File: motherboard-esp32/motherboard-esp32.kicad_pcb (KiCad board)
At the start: 4 copper layers, 300 x 70 mm, 42 parts, among them J3 JST_2P_XH, Q1 DOD4185, Q2 DOD4185, Q3 DOD4185, U1 LMR23630AFDDAR, U2 LM25085MY/NOPB

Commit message: split into two boards for dc/dc converter
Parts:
- removed C10: 1nF, bio-robot:C_0603_1608Metric
- removed C11: 3.3nF, bio-robot:C_0603_1608Metric
- removed C12: 47uF, bio-robot:CAP_EEEFT1H470AP
- removed C7, C8: 22u_1206, bots:C_1206_3216Metric
- removed C9: 0.47u, bio-robot:C_0603_1608Metric
- removed D2: STPS20M100SG-TR, bio-robot:TO-263-2
- removed L2: 3.3uH, bio-robot:IND_MDA1050-3R3M
- removed Q3: DOD4185, bio-robot:DPAK-3_ONS
- removed R3: 113k, bio-robot:R_0603_1608Metric
- removed R4: 4.12k, bio-robot:R_0603_1608Metric
- removed R5: 10m, bio-robot:R_0805_2012Metric
- removed R8: 10k, bio-robot:R_0603_1608Metric
- removed R9: 2.26k, bio-robot:R_0603_1608Metric
- removed U2: LM25085MY/NOPB, bio-robot:MSOP8_PowerPad
- added H5: MountingHoleM3, MountingHole:MountingHole_3.2mm_M3_DIN965_Pad, F.Cu at (169.5, 29.0)
- added H6: MountingHoleM3, MountingHole:MountingHole_3.2mm_M3_DIN965_Pad, F.Cu at (169.5, 59.0)
- added H7: MountingHoleM3, MountingHole:MountingHole_3.2mm_M3_DIN965_Pad, F.Cu at (144.5, 29.0)
- added H8: MountingHoleM3, MountingHole:MountingHole_3.2mm_M3_DIN965_Pad, F.Cu at (144.5, 59.0)
- added P1: 1.8mm_16AWG, bio-robot:SolderPad_TH_16AWG_1.8mm, F.Cu at (143.5, 39.0)
- added P2: 1.8mm_16AWG, bio-robot:SolderPad_TH_16AWG_1.8mm, F.Cu at (143.5, 49.5)
- added P3: 1.8mm_16AWG, bio-robot:SolderPad_TH_16AWG_1.8mm, F.Cu at (162.5, 59.5)
- added P4: 1.8mm_16AWG, bio-robot:SolderPad_TH_16AWG_1.8mm, F.Cu at (152.0, 59.5)
- C5: moved to B.Cu
- moved C1 5.18 mm to (147.0, 78.5)
- moved C6 4.92 mm to (160.5, 68.5)
- moved R2 4.03 mm to (158.0, 85.0)
- moved L1 3.69 mm to (150.0, 70.0)
- moved C3 3.35 mm to (159.5, 78.0)
- moved C4 3.35 mm to (149.0, 82.5)
- moved R6 3.35 mm to (149.0, 84.0)
- moved R7 3.35 mm to (152.0, 84.0)
- moved U1 3.35 mm to (154.4, 79.6)
- moved C2 3.16 mm to (165.5, 78.5)
- moved C5 3.15 mm to (151.0, 80.4), turned to 0 degrees
- moved H2 2.50 mm to (54.5, 91.0)
- moved R1 2.24 mm to (158.0, 85.5)
- moved H1 2.00 mm to (54.5, 29.0)
- moved H4 1.58 mm to (343.0, 29.0)
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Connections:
- net Net-(BT1-PadP-) renamed /Power Input/P2+
- net Net-(BT2-PadP-) renamed /Power Input/P3+
- net Net-(BT4-PadP-) renamed /Power Input/P5+
- net Net-(BT5-PadP-) renamed /Power Input/P6+
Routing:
- net /dc-dc/U1_VCC: track 0.00 -> 4.91 mm, vias 0 -> 1
- net GND: vias 0 -> 45
- net /Power Input/VBAT: vias 0 -> 45
- added copper zone on F.Cu, net /Power Input/P2+
- added copper zone on F.Cu, net /Power Input/P3+
- added copper zone on B.Cu, net /Power Input/P5+
- added copper zone on B.Cu, net /Power Input/P6+
- added copper zone on B.Cu, net /Power Input/VBAT
- added copper zone on F.Cu, net /Power Input/VBAT
- added copper zone on B.Cu, net GND
- added copper zone on F.Cu, net GND
- added copper zone on In2.Cu, net GND
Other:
- board size 300 x 70 mm -> 296.5 x 70 mm
- board text added: "6.8V"
- board text added: "GND"
- board text added: "VCC"

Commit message: update
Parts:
- removed BT1, BT2, BT3, BT4, BT5, BT6: Keystone_254_BatteryClip_Holder, bio-robot:BAT_254_18650_Holder
- removed R7: 22.1k, bio-robot:R_0603_1608Metric
- added BT8: Keystone_1048P_DualBatteryHolder, bio-robot:BAT_1048P, F.Cu at (97.0, 39.5)
- added D2: SMAZ3V6, bots:D_SMA, F.Cu at (157.6, 52.5)
- added F1: 0437005.WR, bio-robot:Fuse_1206_3216Metric, F.Cu at (141.2, 54.3)
- added J2: Screw_Terminal_01x02, bio-robot:TerminalBlock_MaiXu_MX126-5.0-02P_1x02_P5.00mm, F.Cu at (167.2, 55.8)
- added J4: JST_2P_XH, bio-robot:JST_B2B-XH-A_LF__SN_, F.Cu at (71.5, 91.0)
- added J5: Screw_Terminal_01x02, bio-robot:TerminalBlock_MaiXu_MX126-5.0-02P_1x02_P5.00mm, F.Cu at (167.3, 67.2)
- added J6: Screw_Terminal_01x02, bio-robot:TerminalBlock_MaiXu_MX126-5.0-02P_1x02_P5.00mm, F.Cu at (167.3, 78.8)
- added J7: XT60, bio-robot:AMASS_XT60PW-M, F.Cu at (61.5, 77.8)
- added Q3: DOD4185, bio-robot:DPAK-3_ONS, F.Cu at (147.6, 51.7)
- added Q4: DOD4185, bio-robot:DPAK-3_ONS, F.Cu at (167.1, 48.5)
- added R3: 100k, bio-robot:R_0603_1608Metric, F.Cu at (154.4, 57.8)
- added R4: 100k, bio-robot:R_0603_1608Metric, F.Cu at (154.0, 46.8)
- added R5: 88.7k, bio-robot:R_0603_1608Metric, F.Cu at (153.1, 43.3)
- C1: value 0.1u -> 25SVPF100M; footprint bio-robot:C_0603_1608Metric -> bio-robot:CAP_25SVPF100M
- C2: value 25SVPF100M -> 10u; footprint bio-robot:CAP_25SVPF100M -> bio-robot:C_0805_2012Metric
- C3: value 10u -> 2.2u
- C4: value 30p -> 0.1u
- C5: value 2.2u -> 30p; footprint bio-robot:C_0805_2012Metric -> bio-robot:C_0603_1608Metric; moved to F.Cu
- H1, H2, H3, H4, H5, H6, H7, H8: footprint MountingHole:MountingHole_3.2mm_M3_DIN965_Pad -> bio-robot:MountingHole_3.2mm_M3_DIN965_Pad
- Q2, R1: moved to F.Cu
- R6: value 88.7k -> 22.1k
- moved J3 278.6 mm to (63.0, 90.7), turned to 0 degrees
- moved H4 172.9 mm to (170.2, 21.5)
- moved H3 172.8 mm to (170.2, 90.5)
- moved R2 71.8 mm to (88.3, 67.5)
- moved Q2 69.9 mm to (101.5, 69.2), turned to -90 degrees
- moved R1 69.6 mm to (88.8, 78.5), turned to 180 degrees
- moved D1 68.6 mm to (91.6, 72.7)
- moved F2 68.5 mm to (75.6, 75.2)
- moved Q1 68.2 mm to (81.8, 72.4)
- moved H7 66.9 mm to (117.2, 90.2), turned to 0 degrees
- moved H5 63.5 mm to (117.2, 65.2), turned to 0 degrees
- moved P1 54.6 mm to (127.2, 91.2), turned to 90 degrees
- moved C1 46.8 mm to (168.8, 37.1)
- moved C4 45.8 mm to (151.3, 36.8), turned to 90 degrees
- moved R6 42.9 mm to (156.2, 41.7)
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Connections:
- C1 pad 1: /dc-dc/BOOT -> +BATT
- C1 pad 2: /dc-dc/LM_OUT -> GND
- C2 pad 1: VCC -> +BATT
- C3 pad 1: VCC -> /dc-dc/U1_VCC
- C4 pad 1: +5V -> /dc-dc/BOOT
- C4 pad 2: /dc-dc/FB -> /dc-dc/LM_OUT
- C5 pad 1: /dc-dc/U1_VCC -> +5V
- C5 pad 2: GND -> /dc-dc/FB
- J3 pad 2: GND -> GNDPWR
- P2 pad 1: GND -> GNDPWR
- P4 pad 1: GND -> GNDPWR
- R6 pad 1: +5V -> /dc-dc/FB
- R6 pad 2: /dc-dc/FB -> GND
- U1 pad 5: VCC -> +BATT
- U1 pad 7: VCC -> +BATT
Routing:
- net +5V: track 0.00 -> 26.4 mm, vias 0 -> 46
- net /Power Input/VGATE_2: track 0.00 -> 24.3 mm, vias 0 -> 3
- net /Power Input/VGATE: track 0.00 -> 24.3 mm, vias 0 -> 3
- net /Power Input/SW2: track 0.00 -> 22.5 mm, vias 0 -> 2
- net /dc-dc/FB: track 0.00 -> 4.72 mm
- net /dc-dc/BOOT: track 0.00 -> 3.69 mm
- net GND: track 0.00 -> 1.30 mm, vias 45 -> 64
- net /dc-dc/U1_VCC: track 4.91 -> 5.57 mm, vias 1 -> 0
- net /Power Input/VBAT: vias 45 -> 0
- added copper zone on F.Cu, net +5V
- added copper zone on In2.Cu, net +5V
- added copper zone on F.Cu, net +BATT
- added copper zone on F.Cu, net /Power Input/BAT5V_MID
- added copper zone on F.Cu, net /Power Input/FUSE_BAT5V
- added copper zone on F.Cu, net /Power Input/FUSE_VCC
- added copper zone on F.Cu, net /Power Input/VBAT5V
- added copper zone on F.Cu, net /Power Input/VBAT5V_P2
- added copper zone on F.Cu, net /Power Input/VCC_MID
- added copper zone on F.Cu, net /dc-dc/LM_OUT
- added copper zone on In1.Cu, net GND
- removed copper zone on F.Cu, net /Power Input/P2+
- removed copper zone on F.Cu, net /Power Input/P3+
- removed copper zone on B.Cu, net /Power Input/P5+
- removed copper zone on B.Cu, net /Power Input/P6+
- removed copper zone on B.Cu, net /Power Input/VBAT
- removed copper zone on F.Cu, net /Power Input/VBAT
- removed copper zone on B.Cu, net GND
- removed copper zone on In2.Cu, net GND
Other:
- board size 296.5 x 70 mm -> 123.8 x 77 mm

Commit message: update
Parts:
- D1: footprint bio-robot:D_SMA -> bots:D_SMA
- J3, J4: footprint bio-robot:JST_B2B-XH-A_LF__SN_ -> bots:JST_B2B-XH-A_LF__SN_
- Q1, Q2, Q3, Q4: footprint bio-robot:DPAK-3_ONS -> bots:DPAK-3_ONS
- R1, R2, R3, R4: footprint bio-robot:R_0603_1608Metric -> bots:R_0603_1608Metric
- moved J4 26.9 mm to (64.3, 65.1)
- moved J3 26.8 mm to (55.0, 65.2)
- moved P2 24.3 mm to (117.5, 77.7)
- moved P1 21.8 mm to (117.5, 71.7)
- moved P3 5.51 mm to (148.0, 77.7)
- moved P4 1.03 mm to (148.0, 83.7)
- moved Q4 0.25 mm to (167.3, 48.5)
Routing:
- net /Power Input/SW2: track 22.5 -> 108.4 mm, vias 2 -> 4
- net GND: track 1.30 -> 79.9 mm, vias 64 -> 66
- net /Power Input/SW: track 0.00 -> 52.8 mm, vias 0 -> 2
- net GNDPWR: track 0.00 -> 17.1 mm, vias 0 -> 1
- net /Power Input/VGATE: track 24.3 -> 22.0 mm, vias 3 -> 2
- net /Power Input/VGATE_2: track 24.3 -> 22.1 mm, vias 3 -> 2
- net +5V: track 26.4 -> 27.3 mm, vias 46 -> 45
- net VCC: vias 0 -> 45
- added copper zone on F.Cu, net +6.8V
- added copper zone on F.Cu, net /Power Input/VBAT
- added copper zone on In1.Cu, net GNDPWR
- added copper zone on F.Cu, net VCC
- added copper zone on In2.Cu, net VCC
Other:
- outline, holes or cut-outs redrawn
- board text added: "12V_SW"
- board text added: "5V_SW"

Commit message: board files
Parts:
- moved H1 0.71 mm to (54.0, 21.0)
- moved H2 0.71 mm to (54.0, 91.0)
- moved H3 0.71 mm to (170.8, 91.0)
- moved H4 0.71 mm to (170.8, 21.0)
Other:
- outline, holes or cut-outs redrawn
- board text added: "Battery Motherboard MECH 540 / EECE 571M Marine Robotics Group 3: Quiet Bio-inspired Propulsion System Designed By: Henry Bryant Printed on: March 24th, 2026"
- board text added: "This board has two battery inputs. - 5V Rail: 2-Cell 18650 Protected (Li-Ion). Buck to 5V 3A. - 12V Rail: 3-Cell Custom Battery Pack using XT60. Buck to 6.8V, 10A."
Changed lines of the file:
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@@
 	(footprint "bio-robot:MountingHole_3.2mm_M3_DIN965_Pad"
 		(layer "F.Cu")
-		(at 170.25 90.5 90)
+		(at 170.75 91 90)
 		(descr "Mounting Hole 3.2mm, M3, generated by kicad-footprint-generator mountinghole.py")
 		(tags "mountinghole M3 DIN965")
@@
 				(pts
 					(arc
-						(start 170.25 94.5)
-						(mid 170.25 86.5)
-						(end 170.25 94.5)
+						(start 170.75 95)
+						(mid 170.75 87)
+						(end 170.75 95)
 					)
 				)
@@
 	(footprint "bio-robot:MountingHole_3.2mm_M3_DIN965_Pad"
 		(layer "F.Cu")
-		(at 54.5 21.5)
+		(at 54 21)
 		(descr "Mounting Hole 3.2mm, M3, generated by kicad-footprint-generator mountinghole.py")
 		(tags "mountinghole M3 DIN965")
@@
 				(pts
 					(arc
-						(start 50.5 21.5)
-						(mid 58.5 21.5)
-						(end 50.5 21.5)
+						(start 50 21)
+						(mid 58 21)
+						(end 50 21)
 					)
 				)
@@
 	(footprint "bio-robot:MountingHole_3.2mm_M3_DIN965_Pad"
 		(layer "F.Cu")
-		(at 170.25 21.5)
+		(at 170.75 21)
 		(descr "Mounting Hole 3.2mm, M3, generated by kicad-footprint-generator mountinghole.py")
 		(tags "mountinghole M3 DIN965")
 		(property "Reference" "H4"
-			(at 2.699022 2.952848 0)
+			(at 2.25 3.5 0)
 			(layer "F.SilkS")
 			(effects
@@
 				(pts
 					(arc
-						(start 166.25 21.5)
-						(mid 174.25 21.5)
-						(end 166.25 21.5)
+						(start 166.75 21)
+						(mid 174.75 21)
+						(end 166.75 21)
 					)
 				)
@@
 	(footprint "bio-robot:MountingHole_3.2mm_M3_DIN965_Pad"
 		(layer "F.Cu")
-		(at 54.5 90.5)
+		(at 54 91)
 		(descr "Mounting Hole 3.2mm, M3, generated by kicad-footprint-generator mountinghole.py")
 		(tags "mountinghole M3 DIN965")
@@
 				(pts
 					(arc
-						(start 50.5 90.5)
-						(mid 58.5 90.5)
-						(end 50.5 90.5)
+						(start 50 91)
+						(mid 58 91)
+						(end 50 91)
 					)
 				)
@@
 	)
 	(gr_line
-		(start 50.5 21.5)
-		(end 50.5 90.5)
+		(start 50.5 21)
+		(end 50.5 91)
 		(stroke
 			(width 0.1)
@@
 	)
 	(gr_arc
-		(start 50.5 21.5)
-		(mid 51.671573 18.671573)
-		(end 54.5 17.5)
+		(start 50.5 21)
+		(mid 51.525126 18.525126)
+		(end 54 17.5)
 		(stroke
 			(width 0.1)
@@
 	)
 	(gr_arc
-		(start 54.5 94.5)
-		(mid 51.671573 93.328427)
-		(end 50.5 90.5)
+		(start 54 94.5)
+		(mid 51.525126 93.474874)
+		(end 50.5 91)
 		(stroke
-			(width 0.1)
-			(type default)
+			(width 0.15)
+			(type solid)
 		)
 		(layer "Edge.Cuts")
 	)
 	(gr_line
-		(start 54.5 94.5)
-		(end 170.25 94.5)
+		(start 54 94.5)
+		(end 170.75 94.5)
 		(stroke
 			(width 0.1)
@@
 	)
 	(gr_line
-		(start 170.25 17.5)
-		(end 54.5 17.5)
+		(start 170.75 17.5)
+		(end 54 17.5)
 		(stroke
 			(width 0.1)
@@
 	)
 	(gr_arc
-		(start 170.25 17.5)
-		(mid 173.078427 18.671573)
-		(end 174.25 21.5)
+		(start 170.75 17.5)
+		(mid 173.224874 18.525126)
+		(end 174.25 21)
 		(stroke
 			(width 0.1)
@@
 	)
 	(gr_arc
-		(start 174.25 90.5)
-		(mid 173.078427 93.328427)
-		(end 170.25 94.5)
+		(start 174.25 91)
+		(mid 173.224874 93.474874)
+		(end 170.75 94.5)
 		(stroke
 			(width 0.1)
@@
 	)
 	(gr_line
-		(start 174.25 90.5)
-		(end 174.25 21.5)
+		(start 174.25 91)
+		(end 174.25 21)
 		(stroke
 			(width 0.1)
@@
 		(layer "Edge.Cuts")
 	)
+	(gr_text "This board has two battery inputs.\n- 5V Rail: 2-Cell 18650 Protected (Li-Ion). \n	Buck to 5V 3A.\n- 12V Rail: 3-Cell Custom Battery Pack using XT60. \n	Buck to 6.8V, 10A."
+		(at 71.5 91.25 0)
+		(layer "F.SilkS")
+		(effects
+			(font
+				(size 1 1)
+				(thickness 0.15)
+			)
+			(justify left bottom)
+		)
+	)
 	(gr_text "6.8V"
 		(at 146.75 75.5 0)
@@
 		)
 	)
+	(gr_text "Battery Motherboard\nMECH 540 / EECE 571M Marine Robotics\nGroup 3: Quiet Bio-inspired Propulsion System\nDesigned By: Henry Bryant\nPrinted on: March 24th, 2026"
+		(at 106.25 29.75 0)
+		(layer "B.SilkS")
+		(effects
+			(font
+				(size 1 1)
+				(thickness 0.15)
+			)
+			(justify left bottom mirror)
+		)
+	)

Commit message: update to silkscreen
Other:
- board text added: "12V"
- board text added: "5V"
- board text added: "GNDPWR"
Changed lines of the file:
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@@
 		(tags "THT terminal block MaiXu MX126-5.0-02P pitch 5mm size 10.5x7.8mm drill 1.3mm pad 2.8mm")
 		(property "Reference" "J6"
-			(at 2.25 -5.12 90)
+			(at 2.25 5.2825 90)
 			(layer "F.SilkS")
 			(effects
@@
 		(tags "THT terminal block MaiXu MX126-5.0-02P pitch 5mm size 10.5x7.8mm drill 1.3mm pad 2.8mm")
 		(property "Reference" "J2"
-			(at 2.25 -5.12 270)
+			(at 2.25 5.25 270)
 			(layer "F.SilkS")
 			(effects
@@
 		(tags "THT terminal block MaiXu MX126-5.0-02P pitch 5mm size 10.5x7.8mm drill 1.3mm pad 2.8mm")
 		(property "Reference" "J5"
-			(at 2.25 -5.12 90)
+			(at 2.25 5.315 90)
 			(layer "F.SilkS")
 			(effects
@@
 		(layer "F.SilkS")
 		(effects
+			(font
+				(size 1 1)
+				(thickness 0.15)
+			)
+			(justify left bottom)
+		)
+	)
+	(gr_text "5V"
+		(at 173.489317 57.759759 90)
+		(layer "F.SilkS")
+		(effects
+			(font
+				(size 1 1)
+				(thickness 0.15)
+			)
+			(justify left bottom)
+		)
+	)
+	(gr_text "GND"
+		(at 173.489317 62.088447 90)
+		(layer "F.SilkS")
+		(effects
+			(font
+				(size 1 1)
+				(thickness 0.15)
+			)
+			(justify left bottom)
+		)
+	)
+	(gr_text "6.8V"
+		(at 173.5 69 90)
+		(layer "F.SilkS")
+		(effects
+			(font
+				(size 1 1)
+				(thickness 0.15)
+			)
+			(justify left bottom)
+		)
+	)
+	(gr_text "12V"
+		(at 173.695445 79.678037 90)
+		(layer "F.SilkS")
+		(effects
+			(font
+				(size 1 1)
+				(thickness 0.15)
+			)
+			(justify left bottom)
+		)
+	)
+	(gr_text "GNDPWR"
+		(at 173.75 75.75 90)
+		(layer "F.SilkS")
+		(effects
+			(font
+				(size 1 1)
+				(thickness 0.15)
+			)
+			(justify left bottom)
+		)
+	)
+	(gr_text "GNDPWR"
+		(at 173.75 86.75 90)
+		(layer "F.SilkS")
+		(effects

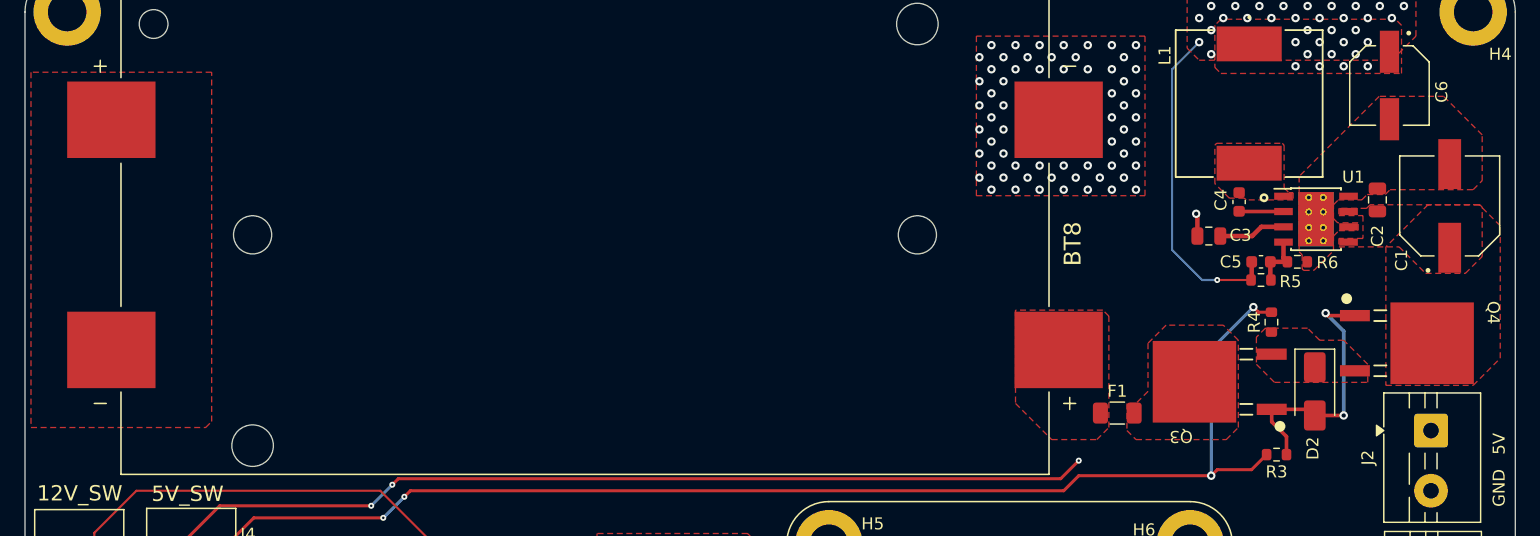
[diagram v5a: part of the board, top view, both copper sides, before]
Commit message: adding leds
- need to add UVLO
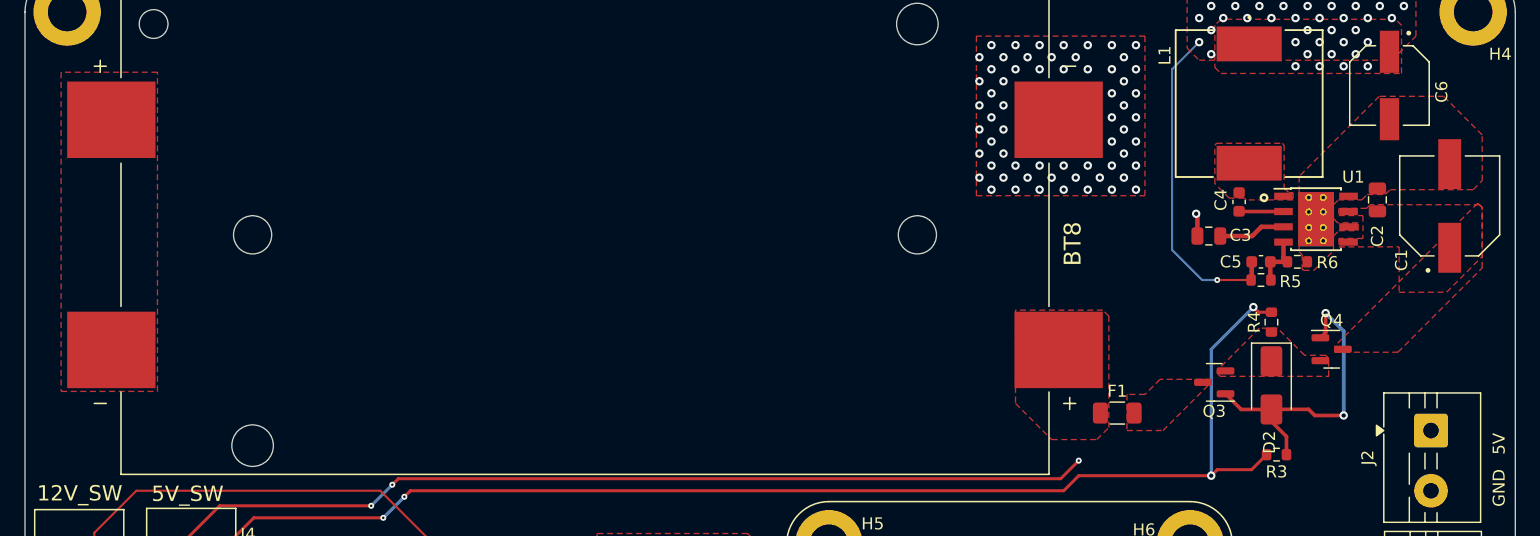
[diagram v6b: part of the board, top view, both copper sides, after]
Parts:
- Q3, Q4: value DOD4185 -> HL3415A; footprint bots:DPAK-3_ONS -> bio-robot:SOT-23
- moved Q4 8.36 mm to (159.0, 49.0), turned to 0 degrees
- moved D2 3.63 mm to (154.0, 52.0)
- moved Q3 1.64 mm to (149.2, 51.8), turned to 180 degrees
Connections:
- Q3 pad 2: /Power Input/FUSE_BAT5V -> /Power Input/BAT5V_MID
- Q3 pad 3: /Power Input/BAT5V_MID -> /Power Input/FUSE_BAT5V
- Q4 pad 2: +BATT -> /Power Input/BAT5V_MID
- Q4 pad 3: /Power Input/BAT5V_MID -> +BATT
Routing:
- net /Power Input/VGATE_2: track 22.1 -> 26.2 mm
